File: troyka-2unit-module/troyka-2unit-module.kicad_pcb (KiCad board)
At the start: 2 copper layers, 50.8 x 25.4 mm, 9 parts, among them J1 UP (A), J2 DOWN (A)

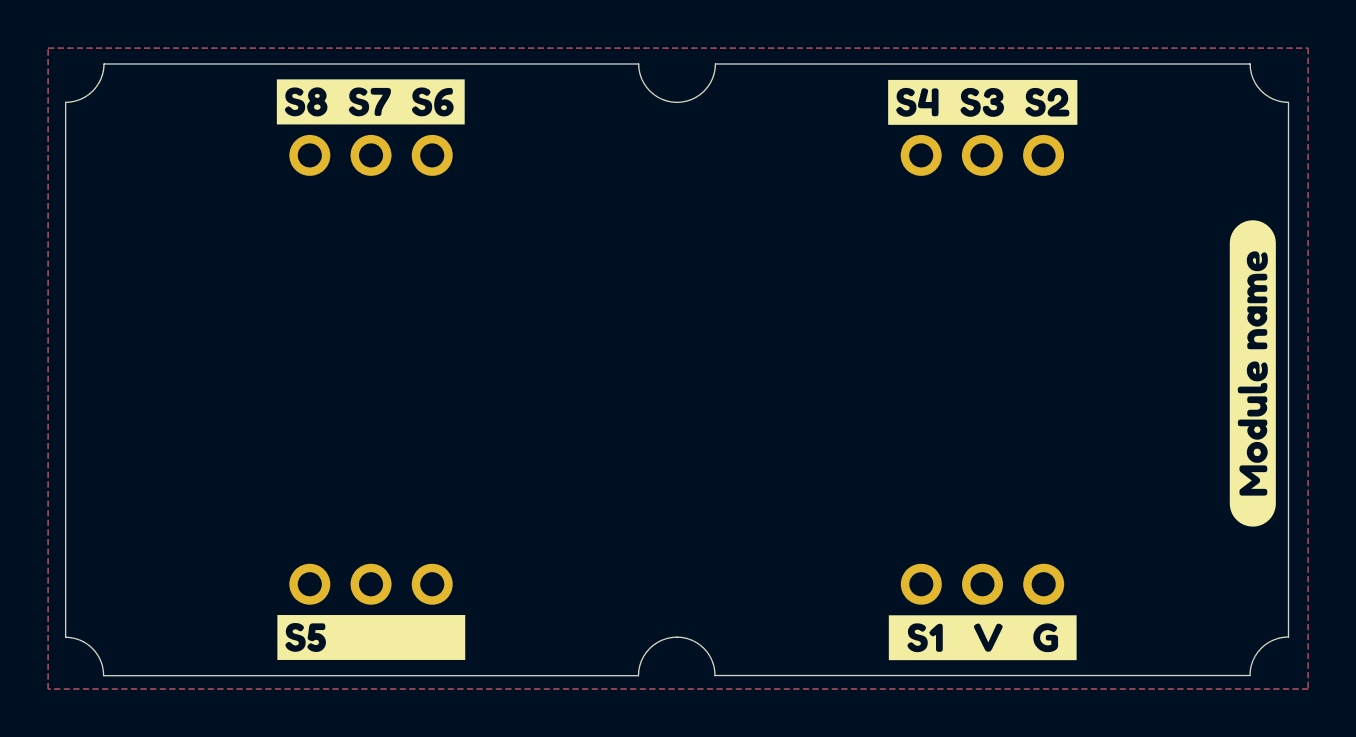
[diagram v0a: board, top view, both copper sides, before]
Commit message: Update templates and CI
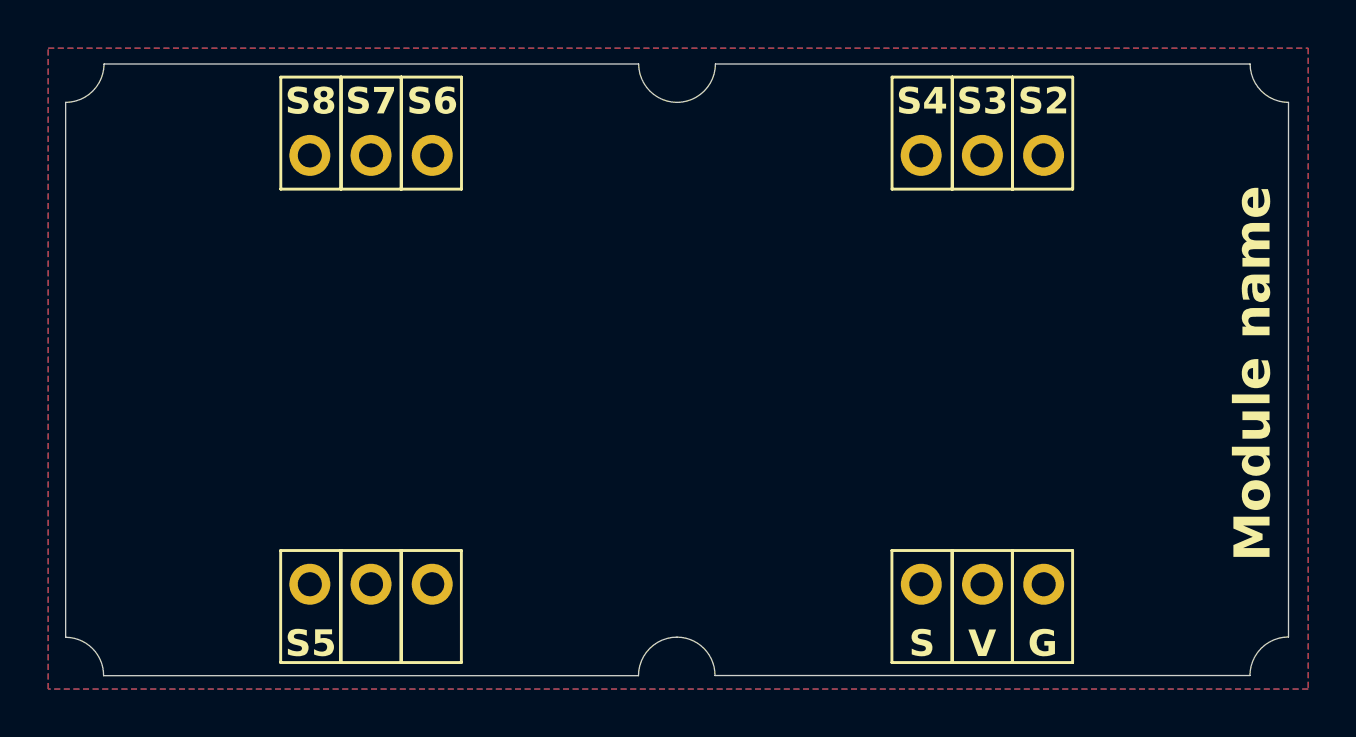
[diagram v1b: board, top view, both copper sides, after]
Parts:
- removed kibuzzard-63E388BB: G***, kibuzzard-63E388BB
- removed kibuzzard-63E38AE1: G***, kibuzzard-63E38AE1
- removed kibuzzard-63E38B38: G***, kibuzzard-63E38B38
- removed kibuzzard-63E38BF1: G***, kibuzzard-63E38BF1
- removed kibuzzard-63E38DFF: G***, kibuzzard-63E38DFF
- renumbered J1 to J3, J2 to J4
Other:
- board text added: "G"
- board text added: "Module name"
- board text added: "S"
- board text added: "S2"
- board text added: "S3"
- board text added: "S4"
- board text added: "S5"
- board text added: "S6"
- board text added: "S7"
- board text added: "S8"
- board text added: "V"
